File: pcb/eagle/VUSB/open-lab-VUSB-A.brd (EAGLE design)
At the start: 64.9 x 52.8 mm, 68 parts, among them IC1 ATMEGA328P, IC2 MCP73831, IC4 MCP1700-33, IC6 MAX31855, IC7 ENC28J60, J1 AYZ0202, Q2 BSS123, U3 BMP085, X1 USBSMD, X2 32.768kHz, X3 25MHz

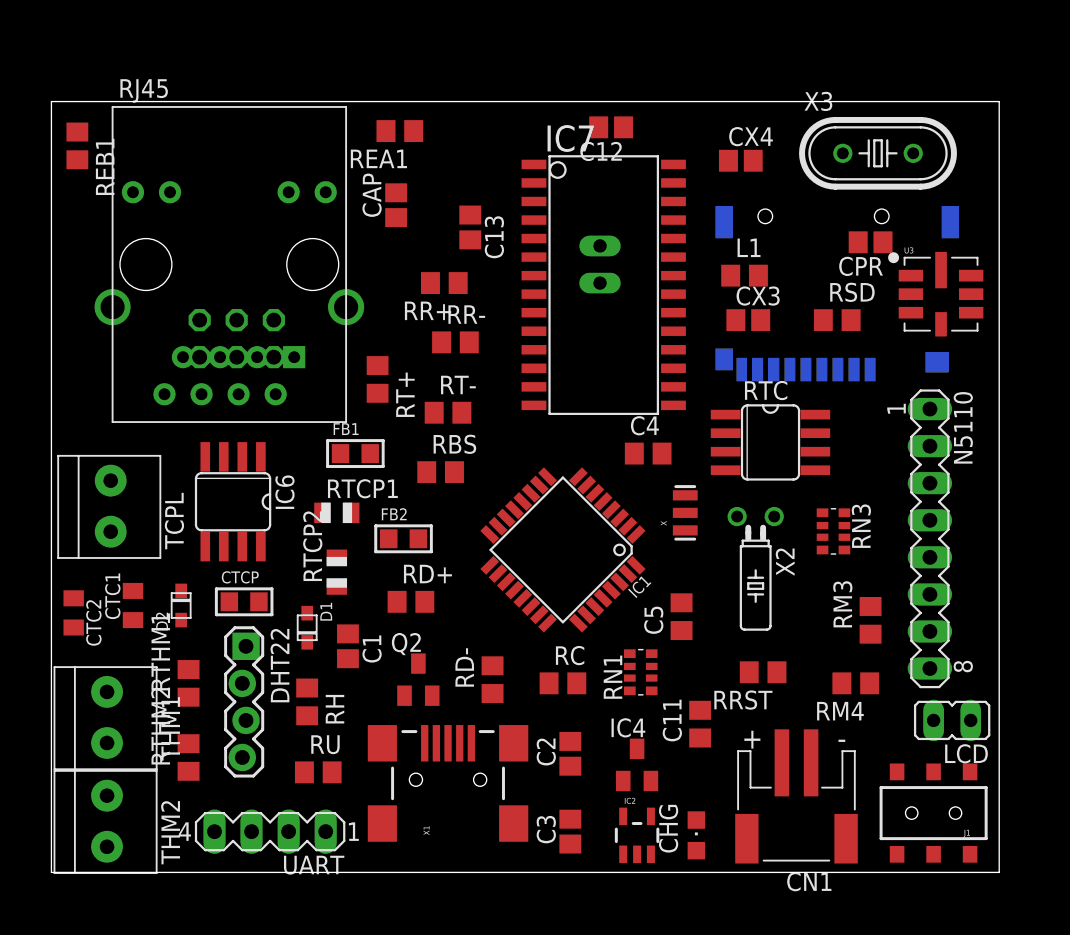
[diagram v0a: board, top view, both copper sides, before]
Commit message: fixed some pin assignments
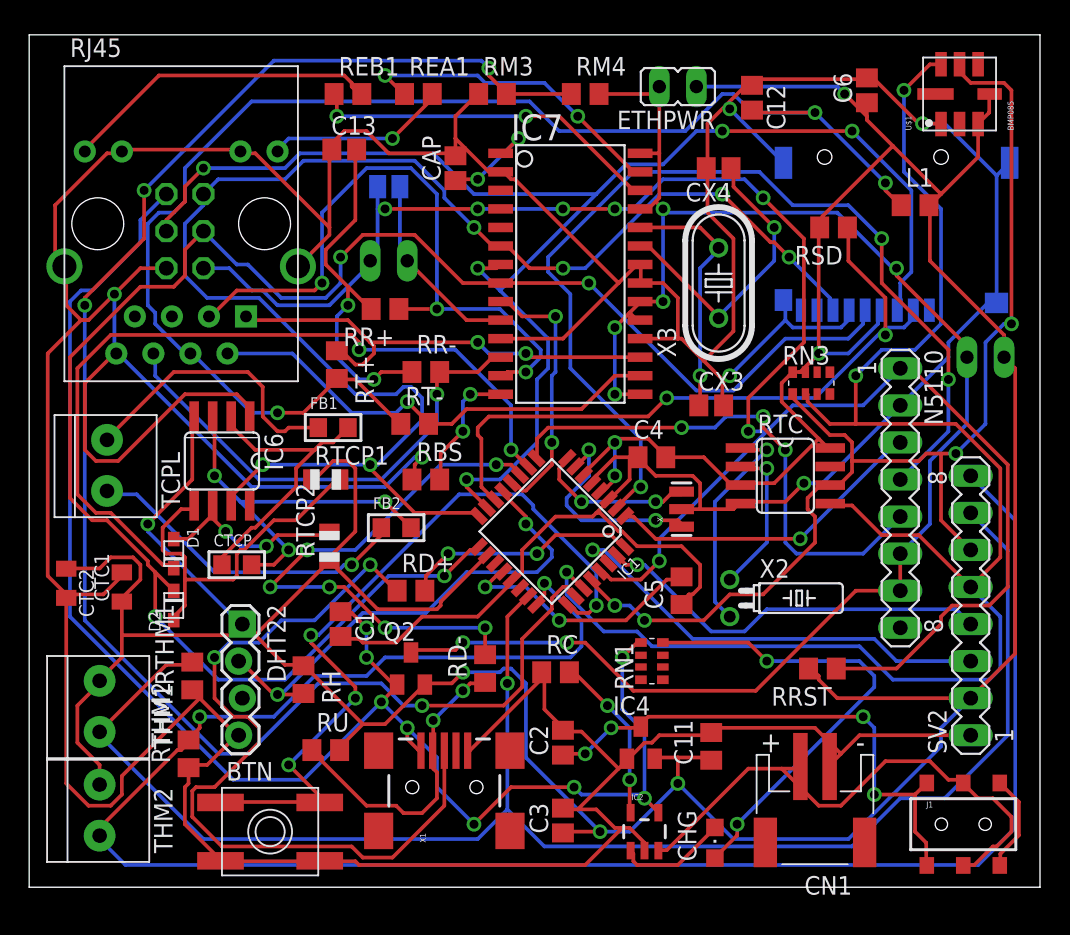
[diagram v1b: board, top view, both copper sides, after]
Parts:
- removed CPR: 1.0uF, adafruit:C0805
- removed ETH: (no value), jumper:JP1
- removed U3: BMP085, microbuilder:BMP085
- removed UART: (no value), con-lstb:MA04-1
- added BTN: (no value), adafruit:EVQ-Q2
- added C6: .1u, resistor:C0805
- added ETHPWR, ETHRESET: (no value), jumper:JP1
- added ETHRESETS: (no value), jumper:SJ
- added SV2: (no value), con-lstb:MA08-1
- added U$1: BMP085, JeeLabs:BMP085
- moved RM4 44.4 mm to (36.6, 53.3), turned to 0 degrees
- moved RM3 44.4 mm to (30.2, 53.3), turned to 0 degrees
- moved LCD 25.0 mm to (64.0, 35.3), flipped to the bottom, turned to 270 degrees
- moved REB1 18.9 mm to (20.3, 53.3), turned to 0 degrees
- moved X3 14.1 mm to (45.7, 40.4), turned to 90 degrees
- moved L1 12.6 mm to (59.2, 45.7)
- moved D1 10.5 mm to (8.38, 21.8)
- moved RN3 10.3 mm to (52.1, 33.5), turned to 0 degrees
- moved C13 10.2 mm to (20.1, 49.5), turned to 0 degrees
- moved C12 9.86 mm to (48.0, 53.1), turned to 270 degrees
- moved ISP 8.18 mm to (9.14, 43.9), turned to 270 degrees
- moved CX3 6.37 mm to (45.2, 32.0)
- moved RSD 6.36 mm to (53.6, 44.2), turned to 180 degrees
- moved X2 5.86 mm to (46.5, 18.8), turned to 270 degrees
- moved MICROSD 5.75 mm to (57.9, 49.0)
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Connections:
- new net ETH_RESET: ETHRESET.1, ETHRESETS.2, IC7.10
- new net N$14: U$1.P$8
- net A0: now also SV2.7
- net A1: now also SV2.8
- net A2: now also BTN.B, BTN.B'; no longer RM3.2, RM4.1
- net A3: now also RM3.2, RM4.1; no longer MICROSD.2, RSD.1
- net D10: now also MICROSD.2, RSD.1
- net D2: no longer N5110.3
- net D3: now also N5110.3; no longer N5110.4
- net D4: now also N5110.4; no longer N5110.5
- net D5: now also N5110.5
- net GND: now also BTN.A, BTN.A', C6.2, SV2.1, U$1.P$1; no longer CPR.2, U3.P$1, UART.1
- net RESET: now also ETHRESET.2, ETHRESETS.1; no longer IC7.10
- net RXD: now also SV2.3; no longer UART.3
- net SCL: now also SV2.6, U$1.P$6; no longer U3.P$6
- net SDA: now also SV2.5, U$1.P$7; no longer U3.P$7
- net TXD: now also SV2.4; no longer UART.4
- net VCC: now also C6.1, ETHPWR.1, SV2.2, U$1.P$3, U$1.P$4; no longer CPR.1, ETH.1, U3.P$3, U3.P$4, UART.2
- net V_CON: now also ETHPWR.2; no longer ETH.2
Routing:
- net GND: track 0.00 -> 463.6 mm, vias 0 -> 6
- net VCC: track 0.00 -> 300.6 mm, vias 0 -> 8
- net A1: track 0.00 -> 136.5 mm, vias 0 -> 2
- net RESET: track 0.00 -> 127.5 mm, vias 0 -> 7
- net SCK: track 0.00 -> 121.4 mm, vias 0 -> 4
- net V_CON: track 0.00 -> 115.0 mm, vias 0 -> 7
- net A3: track 0.00 -> 111.5 mm, vias 0 -> 4
- net A0: track 0.00 -> 110.4 mm, vias 0 -> 1
- net SDA: track 0.00 -> 109.7 mm, vias 0 -> 3
- net VBUS: track 0.00 -> 108.5 mm, vias 0 -> 8
- net MISO: track 0.00 -> 106.1 mm, vias 0 -> 6
- net MOSI: track 0.00 -> 101.2 mm, vias 0 -> 5
- net TCT: track 0.00 -> 95.0 mm, vias 0 -> 3
- net SCL: track 0.00 -> 79.6 mm, vias 0 -> 4
- net D4: track 0.00 -> 67.6 mm, vias 0 -> 3
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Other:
- board size 64.9 x 52.8 mm -> 69.3 x 58.4 mm

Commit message: update
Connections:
- removed net N$14: U$1.P$8
- net VCC: now also U$1.P$8
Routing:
- net RESET: track 127.5 -> 231.2 mm, vias 7 -> 8
- net TCT: track 95.0 -> 174.8 mm, vias 3 -> 8
- net A3: track 111.5 -> 52.4 mm, vias 4 -> 2
- net GND: track 463.6 -> 414.8 mm, vias 6 -> 10
- net VBUS: track 108.5 -> 154.7 mm, vias 8 -> 10
- net SCK: track 121.4 -> 162.9 mm, vias 4 -> 7
- net SDA: track 109.7 -> 72.3 mm, vias 3 -> 6
- net D4: track 67.6 -> 30.8 mm
- net A1: track 136.5 -> 100.7 mm, vias 2 -> 5
- net TD-: track 32.3 -> 65.0 mm, vias 1 -> 2
- net D+: track 55.0 -> 23.6 mm
- net N$11: track 22.8 -> 52.9 mm, vias 1 -> 2
- net D6: track 55.1 -> 28.2 mm
- net A2: track 52.9 -> 29.4 mm, vias 4 -> 2
- net RD+: track 45.9 -> 24.3 mm, vias 3 -> 2
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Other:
- board text added: "+"
- board text added: "A0"
- board text added: "A1"
- board text added: "D3"
- board text added: "D4"
- board text added: "D5"
- board text added: "GND"
- board text added: "MISO"
- board text added: "OpenLabMonitor"
- board text added: "RESET"
- board text added: "RXD"
- board text added: "SCL"
- board text added: "SDA"
- board text added: "T+"
- board text added: "T-"
- board text added: "TXD"
- board text added: "VCC"
- board text added: "VCON"
- board text added: "VUSB-REVA"
